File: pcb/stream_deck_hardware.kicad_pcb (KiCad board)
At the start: 2 copper layers, 70 x 100 mm, 102 parts, among them J2 USB_C_Receptacle_USB2.0, J4 Conn_01x04_Male, J5 Conn_01x05_Male, J6 Conn_01x03_Female, SW1 SW_Push1, SW2 SW_Push2, SW3 SW_Push3, SW4 SW_Push, SW5 SW_Push, SW6 SW_Push, SW7 SW_Push, SW8 SW_Push, SW9 SW_Push, U1 LF33_TO252, U2 STM32F401RCTx, U3 74LVC1G332, U4 AT24CS02-STUM, U5 AT24CS02-STUM, Y1 Crystal_Small

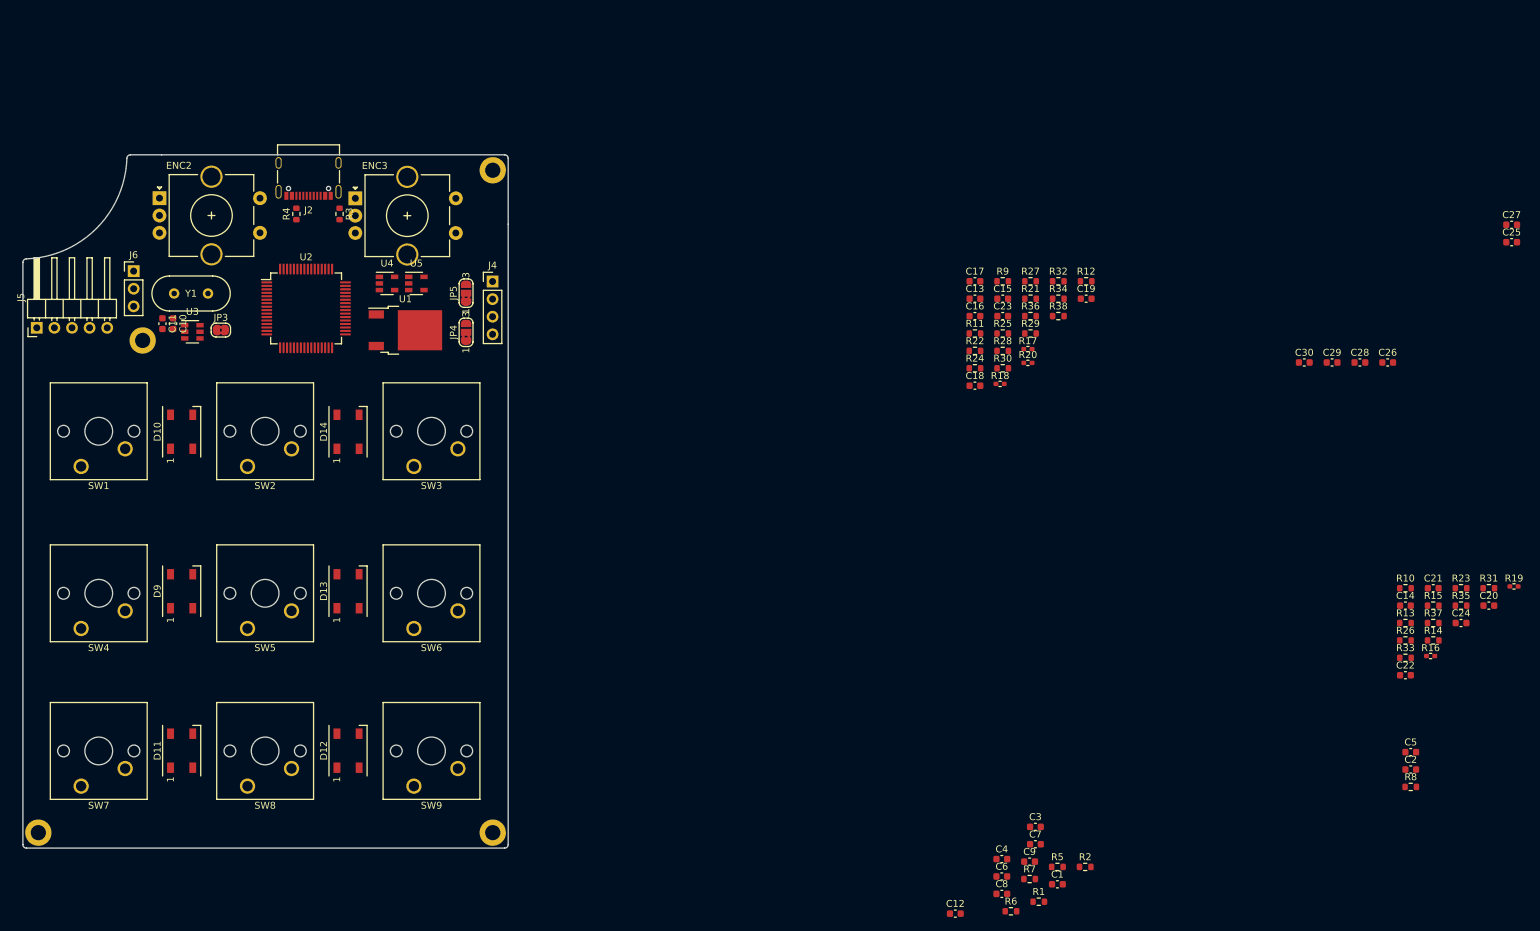
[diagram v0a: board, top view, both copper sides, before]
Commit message: Components placement
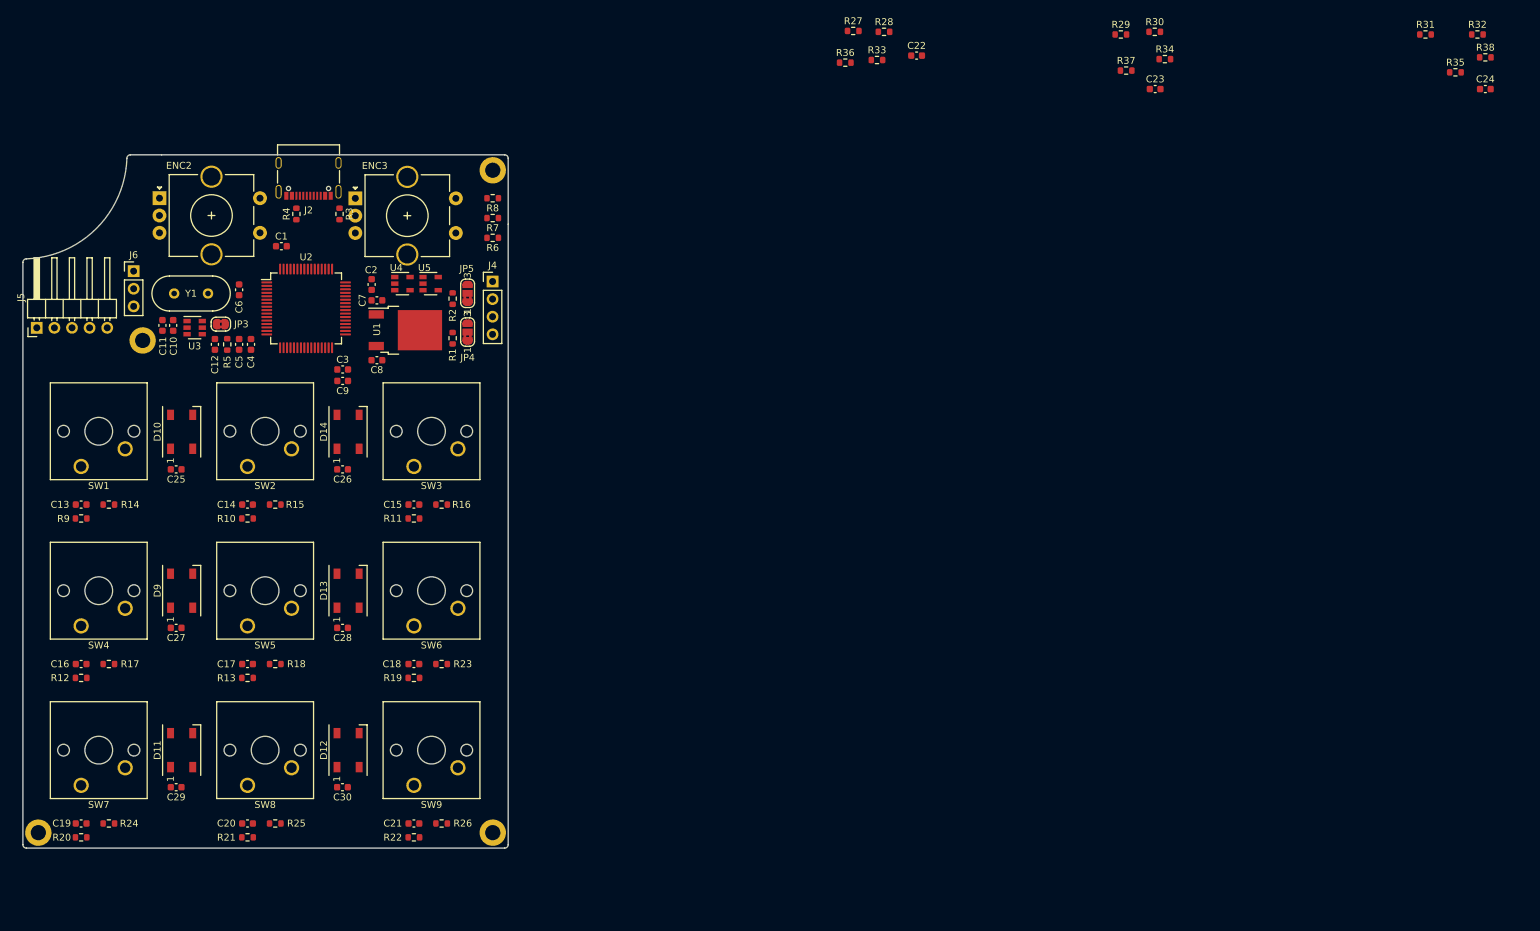
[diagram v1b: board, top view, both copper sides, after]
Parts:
- R16, R17, R18, R19, R20: footprint Resistor_SMD:R_0402_1005Metric_Pad0.72x0.64mm_HandSolder -> Resistor_SMD:R_0603_1608Metric
- moved C27 201.2 mm to (76.7, 113.3), turned to 180 degrees
- moved C25 195.4 mm to (76.7, 90.4), turned to 180 degrees
- moved R14 192.0 mm to (67.0, 95.5)
- moved C20 181.8 mm to (87.0, 141.5), turned to 180 degrees
- moved C5 178.9 mm to (85.8, 72.4), turned to 90 degrees
- moved C29 177.6 mm to (76.7, 136.3), turned to 180 degrees
- moved R15 167.7 mm to (91.0, 95.5)
- moved C14 167.7 mm to (87.0, 95.5), turned to 180 degrees
- moved R10 167.3 mm to (87.0, 97.5)
- moved R13 167.2 mm to (87.0, 120.5)
- moved C2 165.4 mm to (104.9, 63.8), turned to 270 degrees
- moved C19 163.5 mm to (63.0, 141.5), turned to 180 degrees
- moved R19 159.2 mm to (111.0, 120.5)
- moved R8 157.3 mm to (122.4, 51.3), turned to 180 degrees
- moved R12 155.9 mm to (63.0, 120.5)
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
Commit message: Change connectors footprints
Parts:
- added REF**: OSHW-Logo2_14.6x12mm_SilkScreen, Symbol:OSHW-Logo2_14.6x12mm_SilkScreen, B.Cu at (89.5, 97.0)
- added REF**: KiCad-Logo2_8mm_SilkScreen, Symbol:KiCad-Logo2_8mm_SilkScreen, B.Cu at (89.5, 119.7)
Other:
- board text added: "github.com/indamike github.com/lime7git"

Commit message: Pads placement
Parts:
- removed J4: Conn_01x04_Male, Connector_PinHeader_2.54mm:PinHeader_1x04_P2.54mm_Vertical
- removed J5: Conn_01x05_Male, Connector_PinHeader_2.54mm:PinHeader_1x05_P2.54mm_Horizontal
- removed J6: Conn_01x03_Female, Connector_PinHeader_2.54mm:PinHeader_1x03_P2.54mm_Vertical
- added +5V: +5V, TestPoint:TestPoint_Pad_D2.0mm, F.Cu at (71.2, 46.8)
- added +5V: +5V, TestPoint:TestPoint_Pad_D2.0mm, F.Cu at (122.7, 63.8)
- added CLK: SWD CLK, TestPoint:TestPoint_Pad_D2.0mm, F.Cu at (122.7, 66.8)
- added DAT: DATA, TestPoint:TestPoint_Pad_D2.0mm, F.Cu at (70.5, 49.8)
- added DIO: SWD DIO, TestPoint:TestPoint_Pad_D2.0mm, F.Cu at (122.7, 69.8)
- added ENCA: ENC B, TestPoint:TestPoint_Pad_D2.0mm, F.Cu at (65.5, 57.7)
- added ENCB: ENC A, TestPoint:TestPoint_Pad_D2.0mm, F.Cu at (67.7, 55.4)
- added GND: GND, TestPoint:TestPoint_Pad_D2.0mm, F.Cu at (69.4, 52.7)
- added GND: GND, TestPoint:TestPoint_Pad_D2.0mm, F.Cu at (56.3, 61.7)
- added GND: GND, TestPoint:TestPoint_Pad_D2.0mm, F.Cu at (59.6, 61.0)
- added GND: GND, TestPoint:TestPoint_Pad_D2.0mm, F.Cu at (122.7, 72.8)
- added SW: BUTTON, TestPoint:TestPoint_Pad_D2.0mm, F.Cu at (62.7, 59.6)
- JP4, JP5: footprint Jumper:SolderJumper-3_P1.3mm_Bridged2Bar12_RoundedPad1.0x1.5mm_NumberLabels -> Jumper:SolderJumper-3_P1.3mm_Open_RoundedPad1.0x1.5mm
- renumbered J2 to J1

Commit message: Bugfix
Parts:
- renumbered GND to J10, +5V to J11, DAT to J12, GND to J13, +5V to J2, DIO to J3, CLK to J4, GND to J5, ENCB to J6, ENCA to J7, SW to J8, GND to J9
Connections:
- net USB_DM renamed USB_D-
- net USB_DP renamed USB_D+

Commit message: Component placement version 1.0
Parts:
- moved R32 198.5 mm to (70.8, 71.1)
- moved R38 197.8 mm to (70.8, 65.4)
- moved C24 197.4 mm to (70.8, 67.3), turned to 180 degrees
- moved R35 193.9 mm to (70.8, 69.2)
- moved R31 191.6 mm to (70.8, 73.0), turned to 180 degrees
- moved R30 159.3 mm to (64.8, 71.1)
- moved R34 159.2 mm to (64.8, 69.2)
- moved C23 156.4 mm to (64.8, 67.3), turned to 180 degrees
- moved R29 155.0 mm to (64.8, 73.0), turned to 180 degrees
- moved R37 152.5 mm to (64.8, 65.4)
- moved C22 130.0 mm to (58.8, 67.3), turned to 180 degrees
- moved R28 127.8 mm to (58.8, 71.1)
- moved R33 124.9 mm to (58.8, 69.2)
- moved R27 124.4 mm to (58.8, 73.0), turned to 180 degrees
- moved R36 119.3 mm to (58.8, 65.4)
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
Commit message: commit
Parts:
- added REF**: SW_PUSH_6mm, Button_Switch_THT:SW_PUSH_6mm, F.Cu at (110.1, 132.8)
- added REF**: SW_PUSH_6mm, Button_Switch_THT:SW_PUSH_6mm, F.Cu at (86.1, 132.8)
- added REF**: SW_PUSH_6mm, Button_Switch_THT:SW_PUSH_6mm, F.Cu at (62.1, 132.8)
- added REF**: SW_PUSH_6mm, Button_Switch_THT:SW_PUSH_6mm, F.Cu at (110.1, 109.8)
- added REF**: SW_PUSH_6mm, Button_Switch_THT:SW_PUSH_6mm, F.Cu at (86.1, 109.8)
- added REF**: SW_PUSH_6mm, Button_Switch_THT:SW_PUSH_6mm, F.Cu at (62.1, 109.8)
- added REF**: SW_PUSH_6mm, Button_Switch_THT:SW_PUSH_6mm, F.Cu at (110.1, 86.8)
- added REF**: SW_PUSH_6mm, Button_Switch_THT:SW_PUSH_6mm, F.Cu at (86.1, 86.8)
- added REF**: SW_PUSH_6mm, Button_Switch_THT:SW_PUSH_6mm, F.Cu at (62.1, 86.8)

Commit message: COMPONENT PLACEMENT
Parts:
- removed J2: +5V, TestPoint:TestPoint_Pad_D2.0mm
- removed J3: SWD DIO, TestPoint:TestPoint_Pad_D2.0mm
- removed J4: SWD CLK, TestPoint:TestPoint_Pad_D2.0mm
- removed J5: GND, TestPoint:TestPoint_Pad_D2.0mm
- added 3V3: 3.3V, TestPoint:TestPoint_Pad_D2.0mm, F.Cu at (109.2, 75.7)
- added D+: D+, TestPoint:TestPoint_Pad_D2.0mm, F.Cu at (99.3, 56.9)
- added D-: D-, TestPoint:TestPoint_Pad_D2.0mm, F.Cu at (96.3, 56.9)
- added D1: LED, LED_SMD:LED_0805_2012Metric, F.Cu at (122.5, 55.9)
- added D2: 5V_LED, LED_SMD:LED_0805_2012Metric, F.Cu at (122.5, 51.3)
- added D3: 3.3V_LED, LED_SMD:LED_0805_2012Metric, F.Cu at (122.5, 53.6)
- added GND: SCL, TestPoint:TestPoint_Pad_D2.0mm, F.Cu at (77.0, 97.0)
- added GND: SCL, TestPoint:TestPoint_Pad_D2.0mm, F.Cu at (101.3, 97.3)
- added GND: SCL, TestPoint:TestPoint_Pad_D2.0mm, F.Cu at (122.7, 78.7)
- added R39: R, Resistor_SMD:R_0603_1608Metric, F.Cu at (119.4, 55.4)
- added R40: R, Resistor_SMD:R_0603_1608Metric, F.Cu at (119.4, 50.7)
- added R41: R, Resistor_SMD:R_0603_1608Metric, F.Cu at (119.1, 53.1)
- added RST: RESET, Button_Switch_THT:SW_PUSH_6mm, F.Cu at (80.8, 79.0)
- added SWD: SWD, Connector_PinHeader_2.54mm:PinHeader_1x04_P2.54mm_Vertical, F.Cu at (122.3, 64.5)
- added TP3: SDA, TestPoint:TestPoint_Pad_D2.0mm, F.Cu at (123.2, 58.7)
- added TP4: SCL, TestPoint:TestPoint_Pad_D2.0mm, F.Cu at (123.2, 61.5)
- moved R8 6.67 mm to (120.3, 57.7)
- moved R7 5.41 mm to (120.3, 59.2)
- moved C12 5.00 mm to (84.8, 76.7), turned to 0 degrees
- moved R6 4.21 mm to (120.3, 60.7)
- moved C10 0.30 mm to (76.3, 69.4)
- moved C11 0.30 mm to (74.7, 69.4)
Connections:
- J11 pad 1: Net-(J11-Pad1) -> +5V
- J12 pad 1: Net-(J12-Pad1) -> EXTERNAL_LEDS
- J13 pad 1: Net-(J13-Pad1) -> GND

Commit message: puszuje to
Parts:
- ENC3: moved to B.Cu
- moved C4 6.31 mm to (92.7, 76.0), turned to 270 degrees
- moved Y1 4.85 mm to (76.5, 64.8), turned to 0 degrees
- moved C2 4.02 mm to (101.6, 61.5), turned to 90 degrees
- moved R8 3.81 mm to (120.3, 61.5)
- moved C5 3.68 mm to (87.4, 69.1)
- moved TP4 3.05 mm to (123.2, 58.4)
- moved TP3 2.79 mm to (123.2, 61.5)
- moved R3 2.74 mm to (97.5, 53.6)
- moved C6 2.19 mm to (86.6, 62.5), turned to 180 degrees
- moved R29 1.91 mm to (64.8, 71.1)
- moved R30 1.91 mm to (64.8, 73.0)
- moved C10 1.87 mm to (74.4, 69.6)
- moved C11 1.50 mm to (76.2, 69.6)
- moved R7 1.27 mm to (120.3, 57.9)
- moved R6 1.02 mm to (120.3, 59.7)
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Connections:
- REF** pad 1: (no net) -> Net-(C21-Pad1)
- REF** pad 1: (no net) -> Net-(C20-Pad1)
- REF** pad 1: (no net) -> Net-(C19-Pad1)
- REF** pad 1: (no net) -> Net-(C18-Pad1)
- REF** pad 1: (no net) -> Net-(C17-Pad1)
- REF** pad 1: (no net) -> Net-(C16-Pad1)
- REF** pad 1: (no net) -> Net-(C15-Pad1)
- REF** pad 1: (no net) -> Net-(C14-Pad1)
- REF** pad 1: (no net) -> Net-(C13-Pad1)
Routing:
- net +5V: track 0.00 -> 143.0 mm
- net Button_1: track 0.00 -> 45.0 mm, vias 0 -> 2
- net Net-(D11-Pad2): track 0.00 -> 44.7 mm
- net Net-(C23-Pad1): track 0.00 -> 33.1 mm
- net +3V3: track 0.00 -> 32.4 mm
- net ENC_02_A: track 0.00 -> 31.8 mm
- net AMBILIGHT_LEDS: track 0.00 -> 31.0 mm
- net Net-(D12-Pad2): track 0.00 -> 30.4 mm
- net EXTERNAL_LEDS: track 0.00 -> 30.3 mm
- net Net-(D13-Pad2): track 0.00 -> 29.8 mm
- net ENC_02_B: track 0.00 -> 29.2 mm
- net USB_D+: track 0.00 -> 27.8 mm
- net USB_D-: track 0.00 -> 27.1 mm, vias 0 -> 2
- net RST: track 0.00 -> 25.6 mm
- net ENC_01_B: track 0.00 -> 21.0 mm
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- added copper zone on F.Cu, net +3V3
- added copper zone on F.Cu, net +5V
